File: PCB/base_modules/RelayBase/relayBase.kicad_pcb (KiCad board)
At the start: 2 copper layers, 34 x 46.5 mm, 9 parts, among them J1 Conn_01x10_Male, J2 Conn_01x10_Male, SW1 SW_SPST

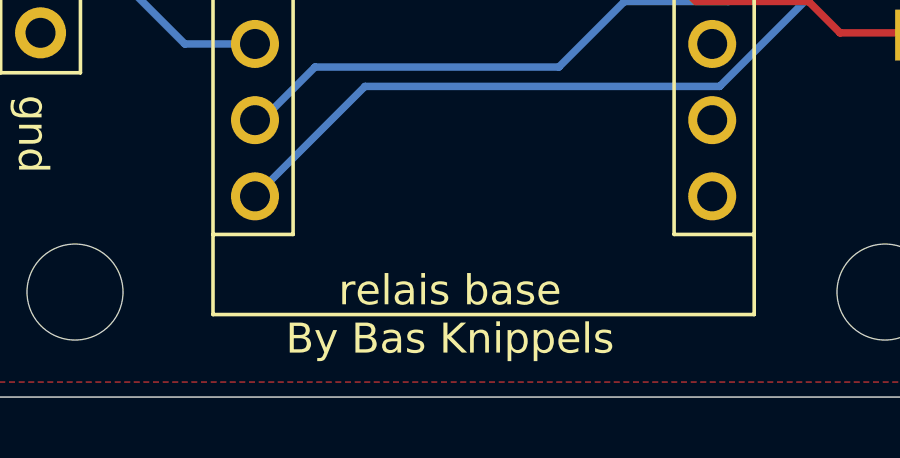
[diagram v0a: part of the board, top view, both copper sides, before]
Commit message: added gerber files in the release folder for all base units. The interfaces are not yet done
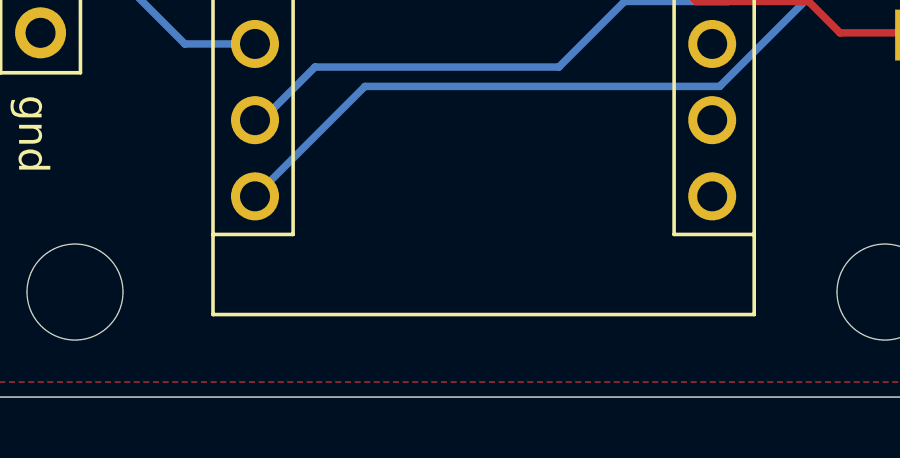
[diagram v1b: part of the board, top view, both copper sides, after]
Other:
- board text added: "Relay base By Bas Knippels"
- board text removed: "relais base By Bas Knippels"
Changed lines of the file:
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@@
-(kicad_pcb (version 20171130) (host pcbnew "(5.1.12)-1")
+(kicad_pcb (version 20171130) (host pcbnew "(5.1.6)-1")
   (general
     (thickness 1.6)
@@
       (outputformat 1)
       (mirror false)
-      (drillshape 1)
+      (drillshape 0)
       (scaleselection 1)
       (outputdirectory ""))
@@
       (effects (font (size 1 1) (thickness 0.15)))
     )
-    (fp_text user %R (at 3.25 2.25) (layer F.Fab)
-      (effects (font (size 1 1) (thickness 0.15)))
-    )
     (fp_line (start 3.25 -0.75) (end 6.25 -0.75) (layer F.Fab) (width 0.1))
     (fp_line (start 6.25 -0.75) (end 6.25 5.25) (layer F.Fab) (width 0.1))
@@
     (fp_line (start 6.75 3) (end 6.75 1.5) (layer F.SilkS) (width 0.12))
     (fp_circle (center 3.25 2.25) (end 1.25 2.5) (layer F.Fab) (width 0.1))
+    (fp_text user %R (at 3.25 2.25) (layer F.Fab)
+      (effects (font (size 1 1) (thickness 0.15)))
+    )
     (pad 1 thru_hole circle (at 6.5 0 270) (size 2 2) (drill 1.1) (layers *.Cu *.Mask)
       (net 13 "Net-(A1-Pad25)"))
@@
     (fp_text value R (at 3.81 1.92 90) (layer F.Fab)
       (effects (font (size 1 1) (thickness 0.15)))
-    )
-    (fp_text user %R (at 3.81 0 90) (layer F.Fab)
-      (effects (font (size 0.72 0.72) (thickness 0.108)))
     )
     (fp_line (start 2.01 -0.8) (end 2.01 0.8) (layer F.Fab) (width 0.1))
@@
     (fp_line (start 8.57 1.05) (end 8.57 -1.05) (layer F.CrtYd) (width 0.05))
     (fp_line (start 8.57 -1.05) (end -0.95 -1.05) (layer F.CrtYd) (width 0.05))
+    (fp_text user %R (at 3.81 0 90) (layer F.Fab)
+      (effects (font (size 0.72 0.72) (thickness 0.108)))
+    )
     (pad 2 thru_hole oval (at 7.62 0 90) (size 1.4 1.4) (drill 0.7) (layers *.Cu *.Mask)
       (net 13 "Net-(A1-Pad25)"))
@@
     (effects (font (size 1 1) (thickness 0.15)))
   )
-  (gr_text "relais base\nBy Bas Knippels" (at 163 116.25) (layer F.SilkS)
-    (effects (font (size 1 1) (thickness 0.15)))
+  (gr_text "Relay base\nBy Bas Knippels" (at 163.5 99.5 90) (layer B.SilkS)
+    (effects (font (size 1 1) (thickness 0.15)) (justify mirror))
   )
   (gr_line (start 147 72.5) (end 147 119) (layer Edge.Cuts) (width 0.05))
